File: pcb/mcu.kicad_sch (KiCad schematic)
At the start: 22 parts, among them J2 AVR-UPDI-UART-6, U4 ATtiny1616-MNR

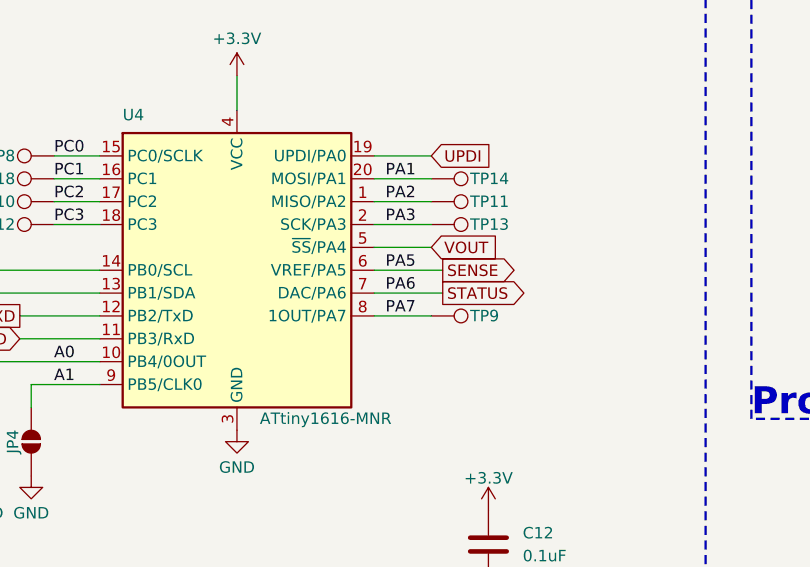
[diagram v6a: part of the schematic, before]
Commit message: Fixed MCU Footprint
Updated renders
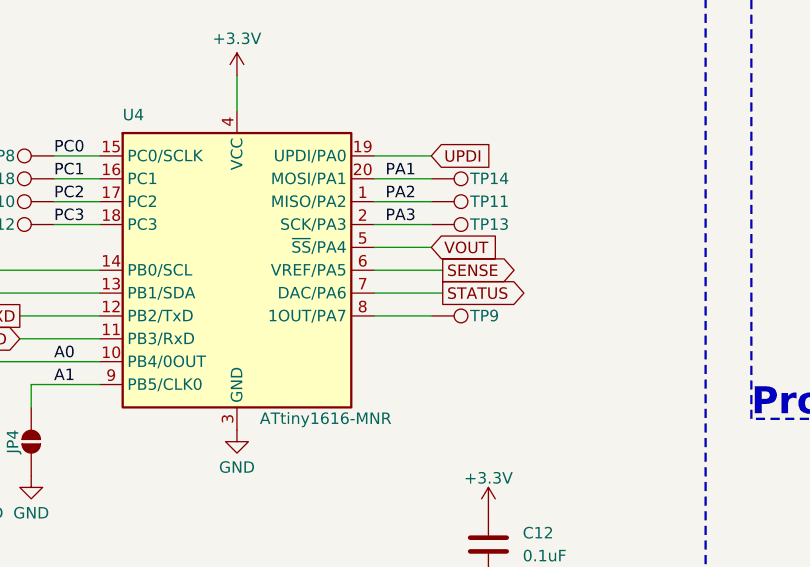
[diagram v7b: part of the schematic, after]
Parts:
- U4: footprint Package_DFN_QFN:VQFN-20-1EP_3x3mm_P0.4mm_EP1.7x1.7mm -> CRG Makes:VQFN-20-1EP_3x3mm_P0.4mm_EP1.7x1.7mm_ThermalVias
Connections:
- net PA7: no longer names the net of TP9.1, U4.8 (1OUT/PA7)
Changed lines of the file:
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@@
 		)
 	)
-	(label "PA7"
-		(at 116.84 62.23 0)
-		(effects
-			(font
-				(size 1.27 1.27)
-			)
-			(justify left bottom)
-		)
-	)
 	(label "PC2"
 		(at 80.01 49.53 0)
@@
 		)
 	)
-	(label "PA6"
-		(at 116.84 59.69 0)
-		(effects
-			(font
-				(size 1.27 1.27)
-			)
-			(justify left bottom)
-		)
-	)
 	(label "A0"
 		(at 80.01 67.31 0)
@@
 		)
 	)
-	(label "PA5"
-		(at 116.84 57.15 0)
-		(effects
-			(font
-				(size 1.27 1.27)
-			)
-			(justify left bottom)
-		)
-	)
 	(global_label "TXD"
 		(shape output)
@@
 			)
 		)
-		(property "Sim.Enable" ""
-			(at 72.39 76.2 0)
-			(effects
-				(font
-					(size 1.27 1.27)
-				)
-				(hide yes)
-			)
-		)
 		(pin "1"
 		)
@@
 			)
 		)
-		(property "Sim.Enable" ""
-			(at 80.01 52.07 90)
-			(effects
-				(font
-					(size 1.27 1.27)
-				)
-				(hide yes)
-			)
-		)
 		(pin "1"
 		)
@@
 			)
 		)
-		(property "Sim.Enable" ""
-			(at 80.01 44.45 90)
-			(effects
-				(font
-					(size 1.27 1.27)
-				)
-				(hide yes)
-			)
-		)
 		(pin "1"
 		)
@@
 			)
 		)
-		(property "Sim.Enable" ""
-			(at 80.01 49.53 90)
-			(effects
-				(font
-					(size 1.27 1.27)
-				)
-				(hide yes)
-			)
-		)
 		(pin "1"
 		)
@@
 			)
 		)
-		(property "Datasheet" "https://optoelectronics.liteon.com/upload/download/DS-22-99-0224/LTST-C190TBKT.PDF"
+		(property "Datasheet" "~"
 			(at 234.95 50.8 0)
 			(effects
@@
 			)
 		)
-		(property "Description" "Blue 120° 3.3V 300mcd 470nm 70mW 0603"
+		(property "Description" "Light emitting diode, small symbol"
 			(at 234.95 50.8 0)
 			(effects
@@
 			)
 		)
-		(property "Sim.Enable" ""
-			(at 234.95 50.8 90)
+		(property "Sim.Pins" "1=K 2=A"
+			(at 234.95 50.8 0)
 			(effects
 				(font
@@
 			)
 		)
-		(property "Sim.Enable" ""
-			(at 64.77 43.18 0)
-			(effects
-				(font
-					(size 1.27 1.27)
-				)
-				(hide yes)
-			)
-		)
 		(pin "2"
 		)
@@
 			)
 		)
-		(property "Sim.Enable" ""
-			(at 128.27 87.63 0)
-			(effects
-				(font
-					(size 1.27 1.27)
-				)
-				(hide yes)
-			)
-		)
 		(pin "1"
 		)
@@
 			)
 		)
-		(property "Sim.Enable" ""
-			(at 252.73 41.91 0)
-			(effects
-				(font
-					(size 1.27 1.27)
-				)
-				(hide yes)
-			)
-		)
 		(pin "1"
 		)
@@
 			)
 		)
-		(property "Sim.Enable" ""
-			(at 177.8 40.64 0)
-			(effects
-				(font
-					(size 1.27 1.27)
-				)
-				(hide yes)
-			)
-		)
 		(pin "1"
 		)
@@
 			)
 		)
-		(property "Sim.Enable" ""
-			(at 64.77 52.07 0)
-			(effects
-				(font
-					(size 1.27 1.27)
-				)
-				(hide yes)
-			)
-		)
 		(pin "2"
 		)
@@
 			)
 		)
-		(property "Sim.Enable" ""
-			(at 121.92 62.23 90)
-			(effects
-				(font
-					(size 1.27 1.27)
-				)
-				(hide yes)
-			)
-		)
 		(pin "1"
 		)
@@
 			)
 		)
-		(property "Sim.Enable" ""
-			(at 234.95 41.91 0)
-			(effects
-				(font
-					(size 1.27 1.27)
-				)
-				(hide yes)
-			)
-		)
 		(pin "1"
 		)
@@
 			)
 		)
-		(property "Sim.Enable" ""
-			(at 49.53 52.07 0)
-			(effects
-				(font
-					(size 1.27 1.27)
-				)
-				(hide yes)
-			)
-		)
 		(pin "2"
 		)
@@
 			)
 		)
-		(property "Sim.Enable" ""
-			(at 121.92 49.53 90)
-			(effects
-				(font
-					(size 1.27 1.27)
-				)
-				(hide yes)
-			)
-		)
 		(pin "1"
 		)
@@
 			)
 		)
-		(property "Sim.Enable" ""
-			(at 49.53 43.18 0)
-			(effects
-				(font
-					(size 1.27 1.27)
-				)
-				(hide yes)
-			)
-		)
 		(pin "2"
 		)
@@
 			)
 		)
-		(property "Sim.Enable" ""
-			(at 121.92 46.99 90)
-			(effects
-				(font
-					(size 1.27 1.27)
-				)
-				(hide yes)
-			)
-		)
 		(pin "1"
 		)
@@
 			)
 		)
-		(property "Sim.Enable" ""
-			(at 80.01 46.99 90)
-			(effects
-				(font
-					(size 1.27 1.27)
-				)
-				(hide yes)
-			)
-		)
 		(pin "1"
 		)
@@
 			)
 		)
-		(property "Sim.Enable" ""
-			(at 121.92 52.07 90)
-			(effects
-				(font
-					(size 1.27 1.27)
-				)
-				(hide yes)
-			)
-		)
 		(pin "1"
 		)
@@
 			)
 		)
-		(property "Footprint" "Package_DFN_QFN:VQFN-20-1EP_3x3mm_P0.4mm_EP1.7x1.7mm"
+		(property "Footprint" "CRG Makes:VQFN-20-1EP_3x3mm_P0.4mm_EP1.7x1.7mm_ThermalVias"
 			(at 99.568 92.71 0)
 			(effects
@@
 			)
 		)
-		(property "Sim.Enable" ""
-			(at 100.33 62.23 0)
-			(effects
-				(font
-					(size 1.27 1.27)
-				)
-				(hide yes)
-			)
-		)
 		(pin "21"
 		)
@@
 			)
 		)
-		(property "Datasheet" "https://optoelectronics.liteon.com/upload/download/DS-22-99-0224/LTST-C190TBKT.PDF"
+		(property "Datasheet" "~"
 			(at 252.73 50.8 0)
 			(effects
@@
 			)
 		)
-		(property "Description" "Blue 120° 3.3V 300mcd 470nm 70mW 0603"
+		(property "Description" "Light emitting diode, small symbol"
 			(at 252.73 50.8 0)
 			(effects
@@
 			)
 		)
-		(property "Sim.Enable" ""
-			(at 252.73 50.8 90)
+		(property "Sim.Pins" "1=K 2=A"
+			(at 252.73 50.8 0)
 			(effects
 				(font
@@
 			)
 		)
-		(property "Sim.Enable" ""
-			(at 77.47 76.2 0)
-			(effects
-				(font
-					(size 1.27 1.27)
-				)
-				(hide yes)
-			)
-		)
 		(pin "1"
 		)
@@
 			(at 190.5 48.26 0)
 			(effects
-				(font
-					(size 1.27 1.27)
-				)
-				(hide yes)
-			)
-		)
-		(property "Sim.Enable" ""
-			(at 190.5 48.26 0)
-			(effects

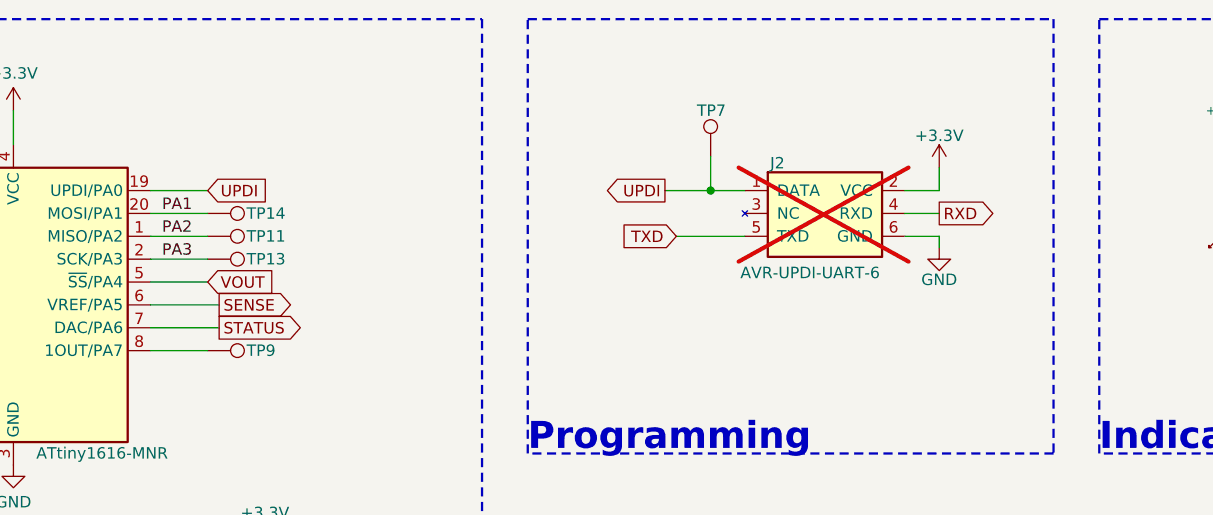
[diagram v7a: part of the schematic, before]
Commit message: Close #1
Added labels to all test points
Moved 3.3 and GND test points
Added labels to top as well as bottom
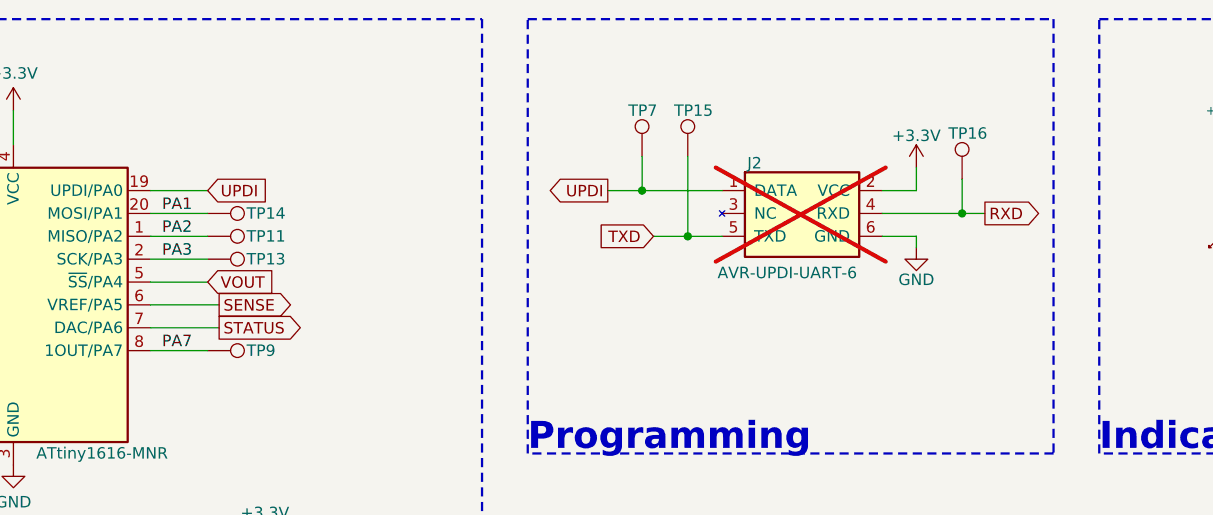
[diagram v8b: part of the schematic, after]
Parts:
- added TP15, TP16: ~, CRGM Mechanical:TestPoint_Pad_D1.0mm, symbol CRGM Connector:TestPoint
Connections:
- net RXD: now also TP16.1
- net TXD: now also TP15.1
- net PA7: now reaches TP9.1, U4.8 (1OUT/PA7)
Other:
- moved on the sheet: J2, TP7
